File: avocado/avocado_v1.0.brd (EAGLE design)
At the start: 76 x 76 mm, 113 parts, among them IC1 TM4C129XXXPDT, IC3 MAX31855, IC4 ISO3088, J1 1X2-3.5MM, U1 LMT87DCKT

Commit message: made significant routing progress
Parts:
- moved R11 24.1 mm to (-1.80, -25.6), flipped to the top
- moved R10 17.9 mm to (13.3, -18.9), flipped to the top
- moved R9 17.0 mm to (17.7, -9.52), flipped to the top
- moved C43 13.3 mm to (25.6, 23.5), turned to 90 degrees
- moved C41 12.7 mm to (24.3, 23.4), turned to 90 degrees
- moved C42 12.0 mm to (22.8, 22.9), turned to 90 degrees
- moved U$7 11.9 mm to (25.7, 11.7)
- moved R6 11.6 mm to (29.6, -9.94), flipped to the top
- moved C34 11.2 mm to (29.1, -8.37), flipped to the top
- moved R16 11.0 mm to (28.9, -11.5), flipped to the top
- moved R15 10.8 mm to (28.9, -12.5), flipped to the top
- moved C8 10.7 mm to (29.8, 17.0), turned to 180 degrees
- moved R38 10.5 mm to (31.0, 11.9), turned to 0 degrees
- moved R8 10.2 mm to (18.0, 14.4), flipped to the top
- moved U$10 10.1 mm to (5.09, -26.7), flipped to the top
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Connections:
- removed net PC7: IC1.22, IC1.23
- removed net PE5: IC1.124
- removed net PK0: IC1.18
- removed net PK1: IC1.19
- removed net PK2: IC1.20
- net PA6: now also U$5.5
- net PC6: now also IC1.22, IC1.23
- net PD5: now also C38.1, U$9.SOA; no longer C40.1, U$9.SOC
- net PD7: now also C40.1, U$9.SOC; no longer C38.1, U$9.SOA
- net PF3: no longer U$9.INLC
- net PF4: no longer U$9.INHC
- net PJ0: no longer U$5.5
- net PP0: now also U$9.INLC
- net PP1: now also U$9.INHC
- net VSENS1: now also IC1.18
- net VSENS2: now also IC1.19
- net VSENS3: now also IC1.20
- net VSENSVM: now also IC1.124
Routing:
- net H3: track 0.00 -> 156.5 mm, vias 0 -> 2
- net H1: track 0.00 -> 153.0 mm, vias 0 -> 2
- net H2: track 0.00 -> 141.9 mm, vias 0 -> 2
- net 3V3DC: track 23.7 -> 126.4 mm, vias 0 -> 1
- net VSENS3: track 0.00 -> 84.5 mm, vias 0 -> 2
- net VSENS1: track 0.00 -> 64.3 mm, vias 0 -> 2
- net NTRST: track 0.00 -> 63.1 mm, vias 0 -> 1
- net GL3: track 0.00 -> 56.7 mm, vias 0 -> 1
- net ISENS3: track 0.00 -> 56.1 mm, vias 0 -> 1
- net VSENS2: track 0.00 -> 53.6 mm, vias 0 -> 2
- net GH3: track 0.00 -> 51.3 mm, vias 0 -> 1
- net SH3: track 0.00 -> 49.6 mm, vias 0 -> 1
- net PA5: track 0.00 -> 44.6 mm
- net PA4: track 0.00 -> 42.6 mm
- net GL2: track 0.00 -> 42.3 mm, vias 0 -> 1
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
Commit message: started Motor traces
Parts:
- moved R11 8.72 mm to (4.76, -19.9), turned to 270 degrees
- moved R4 8.05 mm to (5.75, -32.8)
- moved C14 7.27 mm to (8.18, -31.7), turned to 270 degrees
- moved C7 6.25 mm to (0.89, -26.0), turned to 270 degrees
- moved R36 5.77 mm to (4.54, -31.3)
- moved R35 4.75 mm to (6.67, -31.3), turned to 0 degrees
- moved R10 2.31 mm to (11.0, -19.1)
- moved D2 2.20 mm to (-17.0, -20.2)
- moved U$11 2.10 mm to (18.0, -20.4)
- moved C5 2.01 mm to (18.0, -25.3)
- moved R6 1.62 mm to (31.2, -9.96), turned to 180 degrees
- moved C34 1.40 mm to (30.5, -8.37)
- moved R16 1.20 mm to (30.1, -11.4)
- moved R15 1.10 mm to (30.0, -12.5)
- moved R33 1.00 mm to (-17.0, -18.8)
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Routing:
- net M3: track 1.02 -> 105.2 mm, vias 0 -> 13
- net PB5: track 29.2 -> 133.0 mm, vias 1 -> 4
- net PB4: track 27.8 -> 124.5 mm, vias 1 -> 2
- net M1: track 1.00 -> 91.0 mm, vias 0 -> 15
- net PE4: track 26.6 -> 113.5 mm, vias 1 -> 2
- net M2: track 1.00 -> 79.5 mm, vias 0 -> 11
- net PG0: track 0.00 -> 44.7 mm, vias 0 -> 2
- net VSENS2: track 53.6 -> 79.7 mm, vias 2 -> 3
- net PA0: track 8.31 -> 29.8 mm
- net PA1: track 13.5 -> 34.8 mm
- net 5VDC: track 37.8 -> 57.6 mm, vias 0 -> 1
- net PD4: track 1.84 -> 19.6 mm
- net PP0: track 9.67 -> 26.3 mm, vias 0 -> 2
- net H2: track 141.9 -> 157.9 mm, vias 2 -> 3
- net PP1: track 9.33 -> 24.0 mm, vias 0 -> 2
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- added copper zone on layer 1, net 24VDC
- added copper zone on layer 15, net GND
- added copper zone on layer 1, net ISENS1
- added copper zone on layer 1, net ISENS2
- added copper zone on layer 1, net ISENS3
- added copper zone on layer 1, net M1
- added copper zone on layer 1, net M2
- added copper zone on layer 1, net M3
- removed copper zone on layer 15, net 24VDC
- removed copper zone on layer 2, net GND

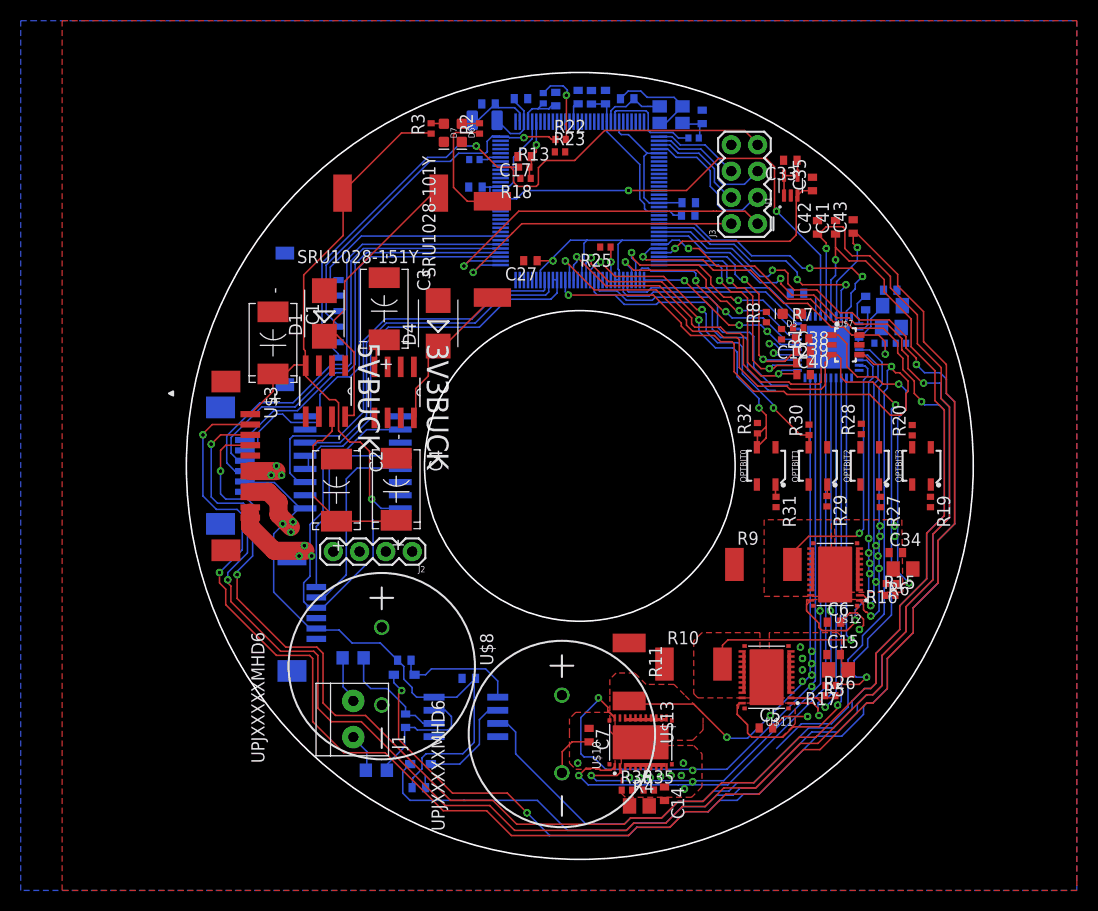
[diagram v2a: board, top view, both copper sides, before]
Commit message: fixed all airwires, still need to fix DRC
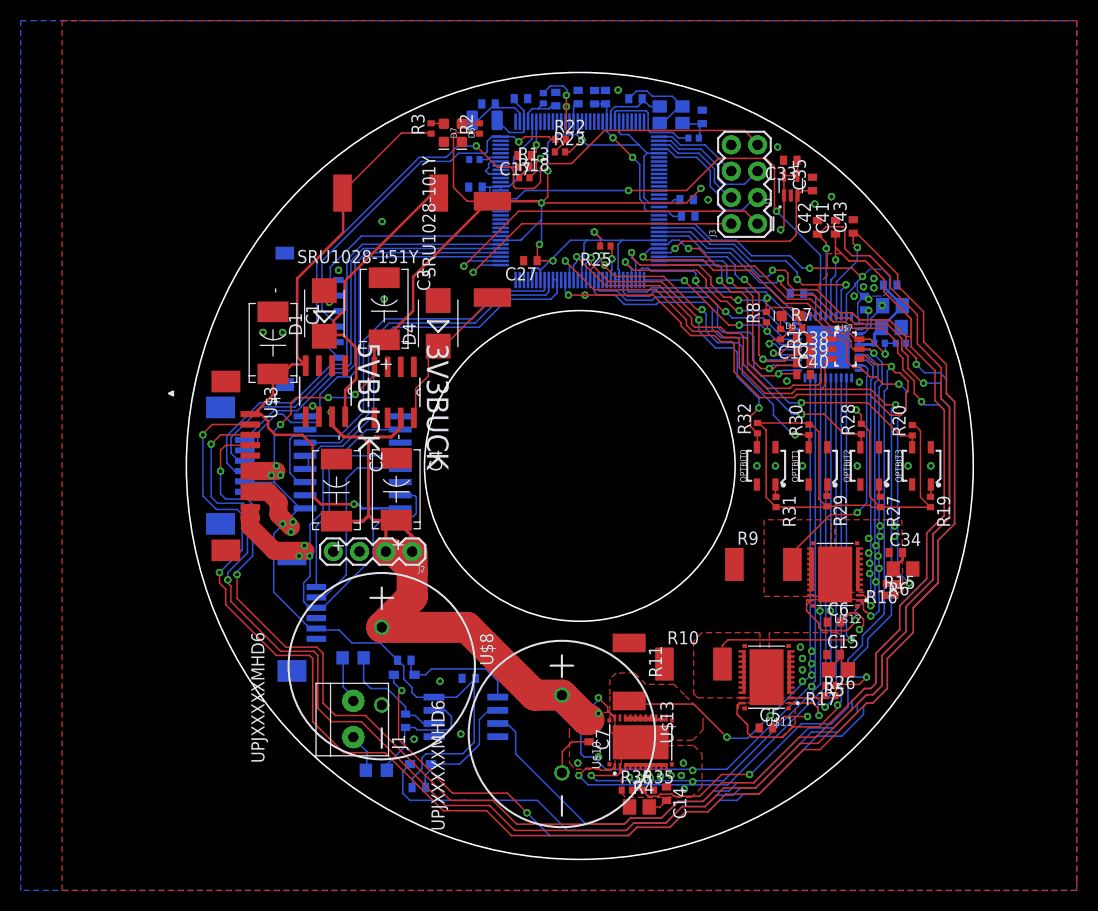
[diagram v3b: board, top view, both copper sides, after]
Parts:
- moved C22 0.80 mm to (5.38, 35.5)
- moved C8 0.50 mm to (30.0, 17.5)
- moved U$7 0.40 mm to (25.7, 11.3)
- moved C28 0.36 mm to (10.3, 25.7)
- moved C21 0.30 mm to (1.42, 35.6)
- moved D5 0.22 mm to (20.4, 14.5)
- moved C14 0.20 mm to (8.38, -31.7)
- moved R18 0.13 mm to (-5.36, 27.8), turned to 0 degrees
- moved C12 0.10 mm to (21.6, 12.3)
- moved R1 0.10 mm to (19.4, 12.7)
- moved R4 0.10 mm to (5.75, -32.9)
- moved R7 0.10 mm to (21.0, 13.3)
- moved C11 0.10 mm to (27.5, 15.7)
- moved C17 0.10 mm to (-5.33, 30.0)
- moved C29 0.10 mm to (10.5, 24.1)
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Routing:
- net 3V3DC: track 131.7 -> 333.1 mm, vias 1 -> 15
- net 24VDC: track 19.7 -> 76.6 mm, vias 4 -> 12
- net VSENS3: track 92.9 -> 109.7 mm, vias 2 -> 3
- net PE3: track 26.3 -> 41.5 mm, vias 0 -> 1
- net PE2: track 25.7 -> 37.0 mm, vias 0 -> 1
- net M1: track 91.0 -> 98.4 mm
- net GND_EXT: track 39.2 -> 46.6 mm
- net M2: track 79.5 -> 84.4 mm
- net ISENS1: track 25.6 -> 29.8 mm
- net GND: track 12.9 -> 16.5 mm, vias 2 -> 28
- net 5VDC: track 57.6 -> 61.1 mm
- net NFAULT: track 2.96 -> 5.97 mm
- net M3: track 105.2 -> 108.2 mm
- net N$22: track 2.40 -> 5.18 mm
- net ISENS3: track 50.2 -> 52.7 mm
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- added copper zone on layer 16, net 24VDC
- added copper zone on layer 2, net 24VDC

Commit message: expanded power and motor traces
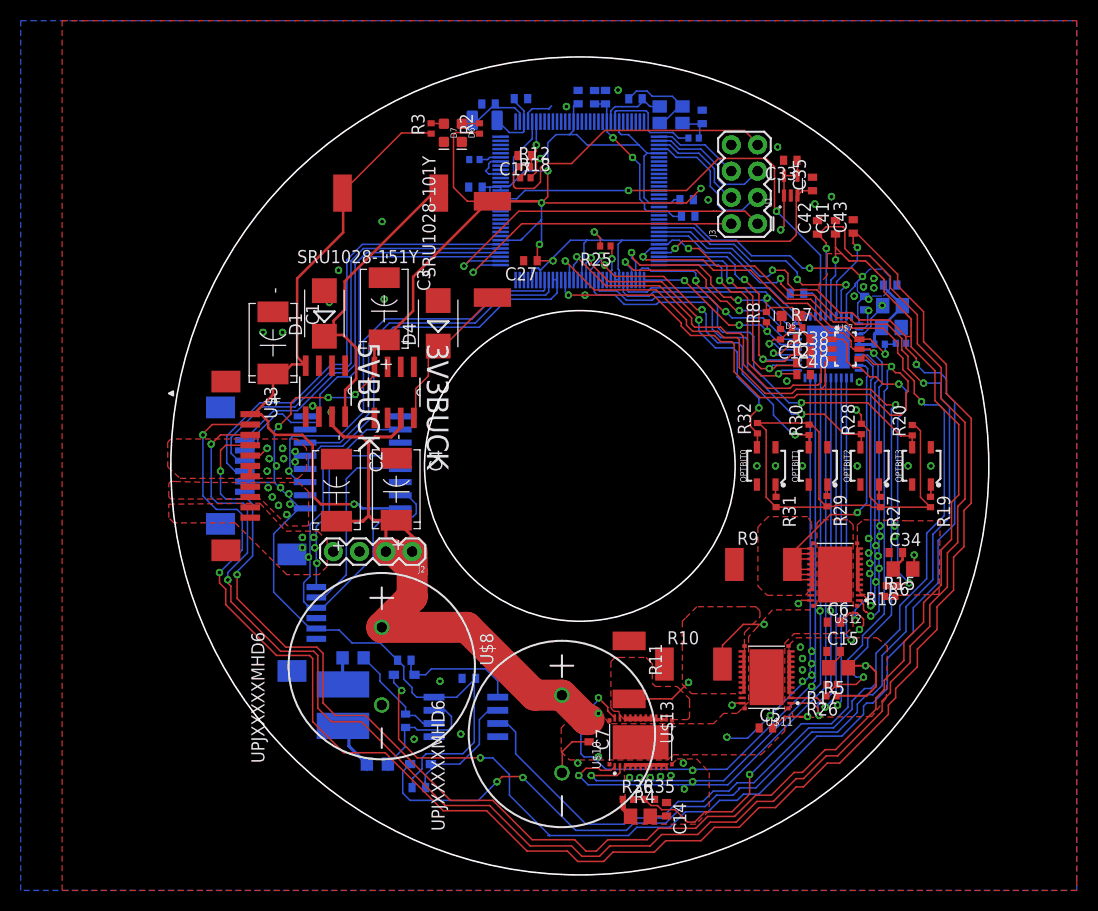
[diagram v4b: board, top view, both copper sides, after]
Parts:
- removed C16: 0.1uF, rcl:C0402
- removed R13: 100, rcl:R0402
- removed R21: 51, rcl:R0402
- removed R22: 1M, rcl:R0402
- removed R23: 0, rcl:R0402
- removed U$5: 5040500691, avocado:5040500691
- added R12: 10K, rcl:R0402
- J1: value 1X2-3.5MM -> THERMOCOUPLE; device adafruit:1X2-3.5MM -> avocado:2_SMP
- moved J1 1.63 mm to (-22.9, -23.1), flipped to the bottom, turned to 90 degrees
- moved C14 1.50 mm to (8.38, -33.2)
- moved R35 0.91 mm to (6.77, -32.2)
- moved R36 0.91 mm to (4.64, -32.2)
- moved R4 0.91 mm to (5.85, -33.8)
- moved FB2 0.61 mm to (-19.6, -28.8)
- moved C15 0.30 mm to (24.5, -17.9)
- moved R11 0.20 mm to (4.76, -19.7)
- moved R16 0.20 mm to (30.1, -11.6)
- moved R5 0.20 mm to (25.0, -19.5)
- moved R17 0.14 mm to (24.3, -21.1)
- moved R26 0.13 mm to (24.3, -22.2), turned to 180 degrees
- moved R15 0.10 mm to (30.0, -12.6)
- moved R18 0.10 mm to (-5.26, 27.8)
- moved R37 0.10 mm to (29.0, 11.8)
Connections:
- removed net N$44: R21.1, R22.2, R23.1
- net 3V3DC: no longer R23.2
- net GND: no longer C16.2, U$5.2, U$5.4, U$5.6
- net NRST: now also R12.2; no longer R13.2
- net NTRST: now also R12.1; no longer R13.1, U$5.1
- net NWAKE: no longer R22.1, U$5.3
- net PA6: no longer U$5.5
- net VBAT: no longer C16.1, R21.2
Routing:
- net M3: track 108.2 -> 56.8 mm, vias 13 -> 17
- net NWAKE: track 36.6 -> 0.75 mm, vias 1 -> 0
- net NTRST: track 64.7 -> 29.6 mm, vias 1 -> 0
- net PA6: track 21.0 -> 0.00 mm
- net M1: track 98.4 -> 78.2 mm, vias 15 -> 18
- net M2: track 84.4 -> 65.0 mm, vias 11 -> 15
- net GND: track 16.5 -> 30.6 mm, vias 28 -> 31
- net N$44: track 9.25 -> 0.00 mm, vias 1 -> 0
- net ISENS1: track 29.8 -> 38.9 mm
- net H3: track 167.9 -> 172.8 mm
- net H1: track 167.5 -> 172.3 mm
- net H2: track 157.9 -> 162.7 mm
- net ISENS3: track 52.7 -> 55.7 mm, vias 1 -> 2
- net VSENS3: track 109.7 -> 112.2 mm
- net 3V3DC: track 333.1 -> 330.9 mm, vias 15 -> 14
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- added copper zone on layer 2, net M1
- added copper zone on layer 2, net M2
- added copper zone on layer 2, net M3
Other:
- board size 76 x 76 mm -> 79 x 79 mm

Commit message: redesigned FET and Cap orientation
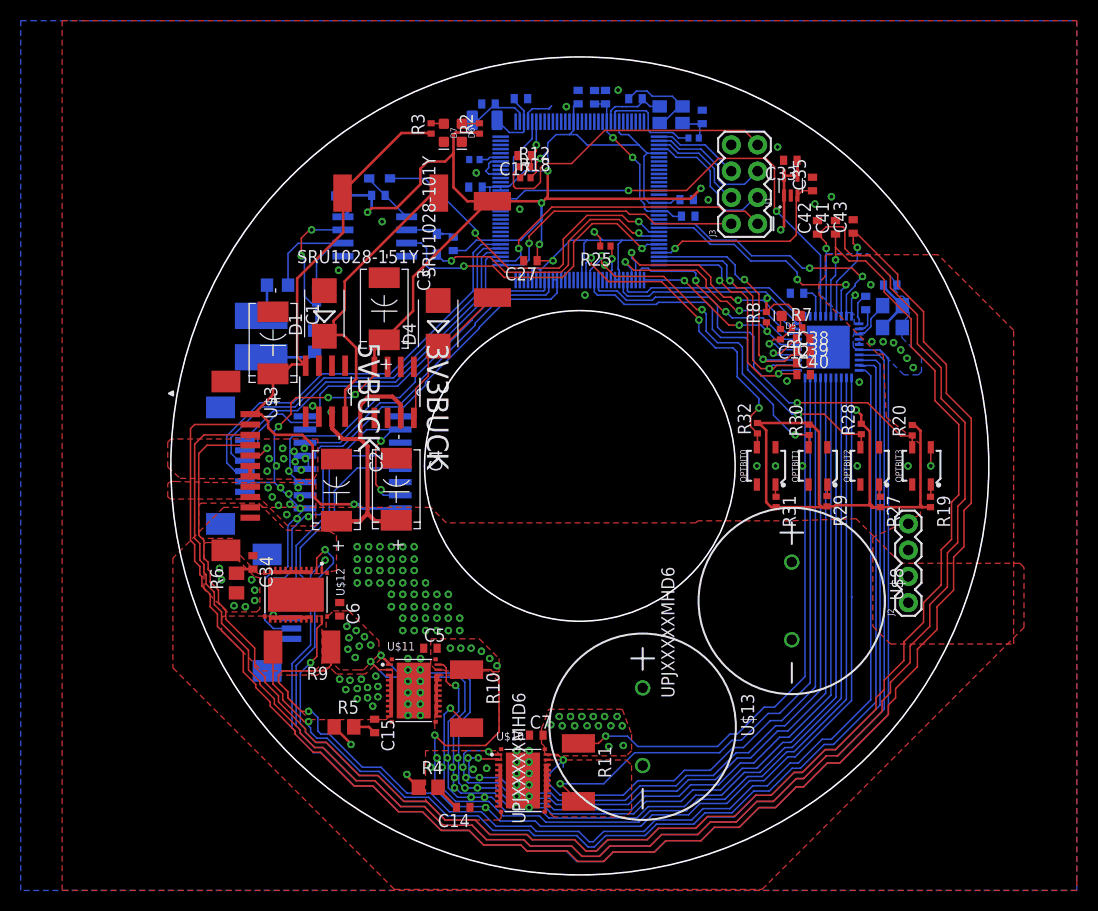
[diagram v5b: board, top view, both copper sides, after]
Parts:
- removed R15, R26, R36, R38: 7.5K, rcl:R0402
- removed R16, R17, R35, R37: 84.5K, rcl:R0402
- removed U$7: TPD4S009, avocado:SOT23-6
- moved R6 64.4 mm to (-33.2, -11.3), turned to 90 degrees
- moved C34 62.1 mm to (-31.6, -9.32), turned to 270 degrees
- moved R34 52.6 mm to (-12.2, 21.5), turned to 90 degrees
- moved U$12 52.1 mm to (-27.4, -12.4), turned to 270 degrees
- moved D3 50.2 mm to (-13.8, 21.4), turned to 270 degrees
- moved C19 48.2 mm to (-23.0, 26.1)
- moved J2 48.2 mm to (31.7, -13.2), turned to 90 degrees
- moved R5 48.1 mm to (-22.8, -25.2), turned to 0 degrees
- moved D2 48.0 mm to (-19.3, 27.8), turned to 180 degrees
- moved C6 47.8 mm to (-23.2, -13.8), turned to 270 degrees
- moved IC3 47.2 mm to (-19.8, 22.2)
- moved R9 45.3 mm to (-26.8, -17.5), turned to 180 degrees
- moved R33 45.0 mm to (-19.5, 26.1)
- moved C15 44.9 mm to (-19.8, -25.1), turned to 270 degrees
- moved C37 41.9 mm to (-25.4, 16.4)
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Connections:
- removed net VSENS1: IC1.18, R15.2, R16.1, U$7.1
- removed net VSENS2: IC1.19, R17.1, R26.2, U$7.3
- removed net VSENS3: IC1.20, R35.1, R36.2, U$7.4
- removed net VSENSVM: IC1.124, R37.1, R38.2, U$7.6
- new net PE5: IC1.124
- new net PK0: IC1.18
- new net PK1: IC1.19
- new net PK2: IC1.20
- net 24VDC: no longer R37.2
- net 3V3DC: no longer U$7.5
- net GND: no longer R15.1, R26.1, R36.1, R38.1, U$7.2
- net M1: no longer R16.2
- net M2: no longer R17.2
- net M3: no longer R35.2
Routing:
- net GND: track 30.6 -> 279.8 mm, vias 31 -> 63
- net VSENS3: track 112.2 -> 0.00 mm, vias 3 -> 0
- net PB5: track 134.6 -> 34.1 mm, vias 4 -> 2
- net PB4: track 126.4 -> 26.6 mm, vias 4 -> 2
- net SH1: track 27.4 -> 125.6 mm
- net GH1: track 30.2 -> 125.2 mm
- net PE4: track 113.5 -> 31.6 mm
- net VSENS2: track 79.2 -> 0.00 mm, vias 3 -> 0
- net M1: track 78.2 -> 0.00 mm, vias 18 -> 0
- net GL1: track 35.4 -> 113.2 mm, vias 2 -> 1
- net ISENS1: track 38.9 -> 112.6 mm
- net VSENS1: track 70.6 -> 0.00 mm, vias 3 -> 0
- net M2: track 65.0 -> 0.00 mm, vias 15 -> 24
- net SH2: track 36.0 -> 96.1 mm
- net GH2: track 37.0 -> 93.4 mm
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- removed copper zone on layer 2, net M1

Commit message: finished DRC and silk for version 1
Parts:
- removed U$1: 0522070633, avocado:1MM-FPC-6PIN
- added U$5: 5040500591, avocado:5040500591
- renumbered 3V3BUCK to U$6, 5VBUCK to U$7, SRU1028-101Y to L2, SRU1028-151Y to L1
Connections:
- net 3V3DC: now also U$5.1; no longer U$1.2
- net A: now also U$5.4; no longer U$1.6
- net B: now also U$5.5; no longer U$1.5
- net GND: now also U$5.2; no longer U$1.3, U$3.THERMPAD, U$3.THERMPAD1
- net GND_EXT: now also U$5.3; no longer U$1.4
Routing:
- net B: track 21.0 -> 17.0 mm
- net ISENS1: track 112.6 -> 110.1 mm
- net GND_EXT: track 41.0 -> 38.6 mm
- net 3V3DC: track 324.8 -> 326.6 mm
- net GND: track 279.8 -> 279.6 mm, vias 63 -> 79
- net 24VDC: vias 80 -> 76
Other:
- board text added: "24V"
- board text added: "5V"
- board text added: "ALLEN AKASH NATHAN RACHEL RYAN TSONG WEILIN"
- board text added: "AVOCADO WILDCAT ROBOT DESIGN STUDIO"
- board text added: "GND"
- board text added: "M1"
- board text added: "NRST"
- board text added: "PA0"
- board text added: "PA1"
- board text added: "SWCLK"
- board text added: "SWDIO"
- board text added: "SWO"
- board text added: "TDI"
